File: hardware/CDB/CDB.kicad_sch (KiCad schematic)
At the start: 17 parts, among them J1 Servo Motor, J2 Bateria, J3 Antena LoRa, Q1 BC547, U1 ESP32-C3, U2 RFM95W, U3 GPS, U4 BMP280, U5 GY-521

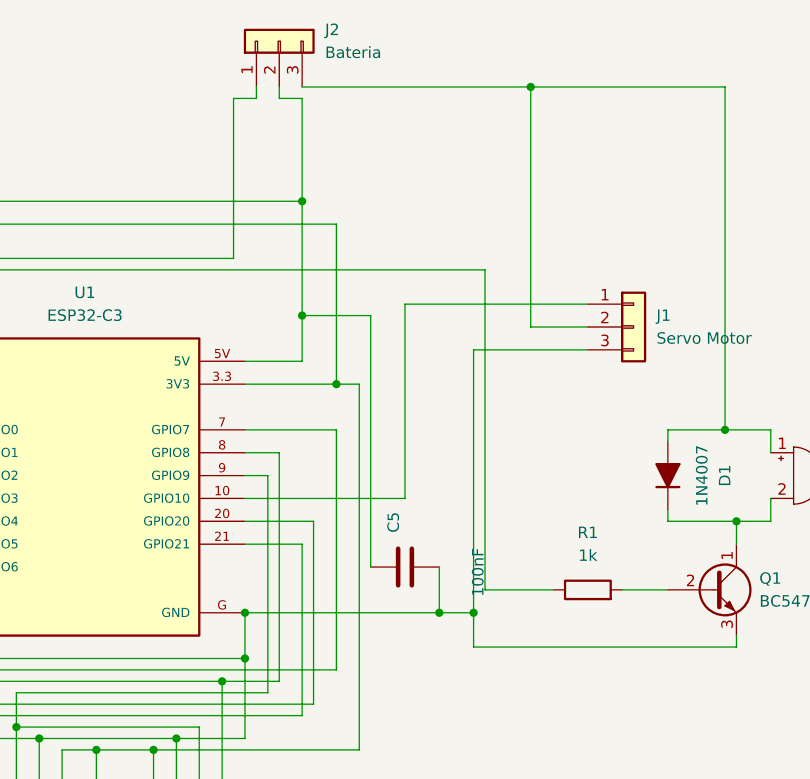
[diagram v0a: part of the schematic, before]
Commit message: add velocity threshold
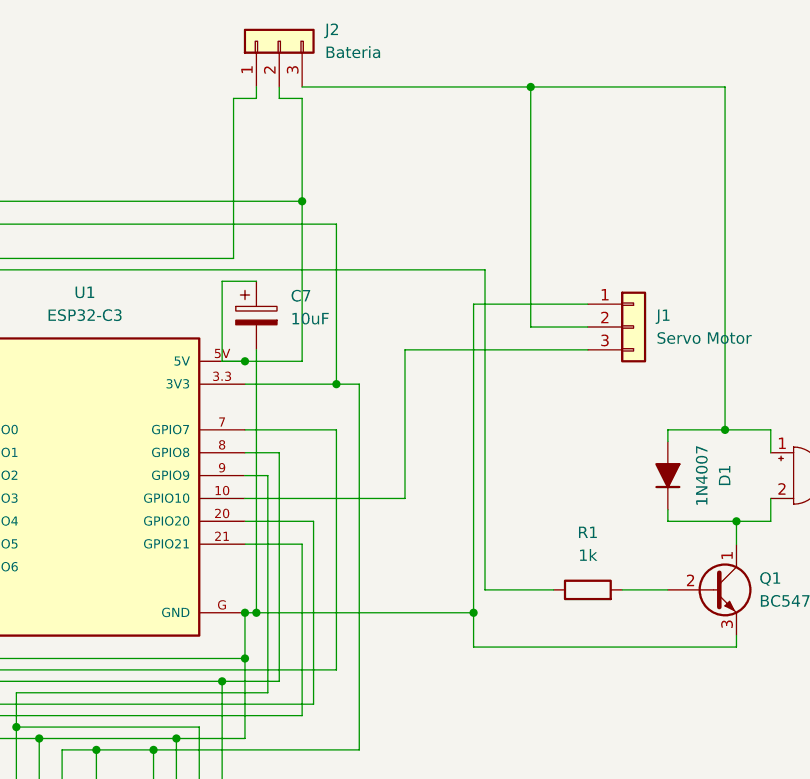
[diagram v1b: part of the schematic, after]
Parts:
- removed C5: 100nF, Capacitor_THT:C_Disc_D4.7mm_W2.5mm_P5.00mm, symbol PCM_Capacitor_AKL:C_Disc_D3.0mm_W1.6mm_P2.50mm
- added C7: 10uF, PCM_Capacitor_THT_AKL:CP_Radial_D4.0mm_P2.00mm, symbol PCM_Capacitor_AKL:CP_Radial_D4.0mm_P2.00mm
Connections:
- net at C1.2, C2.2, C3.2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: now also J1.1 (Pin_1), C7.2; no longer J1.3 (Pin_3)
- net at U1.10 (GPIO10): now also J1.3 (Pin_3); no longer J1.1 (Pin_1)
- net at C1.1, J2.2 (Pin_2), U1.5V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: now also C7.1
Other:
- company: (none) -> Serra Rocketry
- title: Aviônica SR1500 -> Aviônica SRCouto
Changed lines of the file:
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@@
 	(paper "A4")
 	(title_block
-		(title "Aviônica SR1500")
+		(title "Aviônica SRCouto")
 		(date "2025-06-04")
+		(company "Serra Rocketry")
 	)
 	(junction
@@
 	)
 	(junction
-		(at 167.64 71.12)
-		(diameter 0)
-		(color 0 0 0 0)
-	)
-	(junction
 		(at 167.64 58.42)
 		(diameter 0)
@@
 	)
 	(junction
-		(at 151.13 119.38)
+		(at 161.29 76.2)
 		(diameter 0)
 		(color 0 0 0 0)
 	)
 	(junction
-		(at 182.88 104.14)
+		(at 151.13 119.38)
 		(diameter 0)
 		(color 0 0 0 0)
@@
 	)
 	(junction
+		(at 162.56 104.14)
+		(diameter 0)
+		(color 0 0 0 0)
+	)
+	(junction
 		(at 144.78 119.38)
 		(diameter 0)
@@
 	(wire
 		(pts
+			(xy 193.04 72.39) (xy 199.39 72.39)
+		)
+		(stroke
+			(width 0)
+			(type default)
+		)
+	)
+	(wire
+		(pts
 			(xy 104.14 93.98) (xy 80.01 93.98)
 		)
@@
 	(wire
 		(pts
-			(xy 186.69 74.93) (xy 186.69 104.14)
+			(xy 162.56 74.93) (xy 162.56 104.14)
 		)
 		(stroke
@@
 	(wire
 		(pts
+			(xy 179.07 74.93) (xy 199.39 74.93)
+		)
+		(stroke
+			(width 0)
+			(type default)
+		)
+	)
+	(wire
+		(pts
 			(xy 151.13 119.38) (xy 151.13 125.73)
 		)
@@
 	(wire
 		(pts
-			(xy 179.07 91.44) (xy 179.07 69.85)
+			(xy 179.07 91.44) (xy 179.07 74.93)
 		)
 		(stroke
@@
 	(wire
 		(pts
-			(xy 175.26 99.06) (xy 175.26 71.12)
-		)
-		(stroke
-			(width 0)
-			(type default)
-		)
-	)
-	(wire
-		(pts
 			(xy 156.21 116.84) (xy 135.89 116.84)
 		)
@@
 	(wire
 		(pts
-			(xy 161.29 104.14) (xy 182.88 104.14)
-		)
-		(stroke
-			(width 0)
-			(type default)
-		)
-	)
-	(wire
-		(pts
-			(xy 167.64 58.42) (xy 167.64 71.12)
+			(xy 161.29 104.14) (xy 162.56 104.14)
 		)
 		(stroke
@@
 	(wire
 		(pts
-			(xy 179.07 69.85) (xy 199.39 69.85)
-		)
-		(stroke
-			(width 0)
-			(type default)
-		)
-	)
-	(wire
-		(pts
 			(xy 58.42 118.11) (xy 58.42 58.42)
 		)
@@
 	(wire
 		(pts
+			(xy 162.56 104.14) (xy 186.69 104.14)
+		)
+		(stroke
+			(width 0)
+			(type default)
+		)
+	)
+	(wire
+		(pts
 			(xy 138.43 127) (xy 138.43 137.16)
 		)
@@
 	(wire
 		(pts
+			(xy 186.69 69.85) (xy 199.39 69.85)
+		)
+		(stroke
+			(width 0)
+			(type default)
+		)
+	)
+	(wire
+		(pts
 			(xy 165.1 111.76) (xy 165.1 86.36)
 		)
@@
 	(wire
 		(pts
+			(xy 158.75 76.2) (xy 161.29 76.2)
+		)
+		(stroke
+			(width 0)
+			(type default)
+		)
+	)
+	(wire
+		(pts
 			(xy 160.02 64.77) (xy 119.38 64.77)
 		)
@@
 	(wire
 		(pts
+			(xy 158.75 67.31) (xy 158.75 76.2)
+		)
+		(stroke
+			(width 0)
+			(type default)
+		)
+	)
+	(wire
+		(pts
 			(xy 167.64 46.99) (xy 167.64 58.42)
 		)
@@
 	(wire
 		(pts
-			(xy 193.04 72.39) (xy 193.04 45.72)
-		)
-		(stroke
-			(width 0)
-			(type default)
-		)
-	)
-	(wire
-		(pts
 			(xy 63.5 99.06) (xy 118.11 99.06)
 		)
@@
 	(wire
 		(pts
+			(xy 186.69 69.85) (xy 186.69 104.14)
+		)
+		(stroke
+			(width 0)
+			(type default)
+		)
+	)
+	(wire
+		(pts
 			(xy 66.04 135.89) (xy 66.04 118.11)
 		)
@@
 	(wire
 		(pts
-			(xy 182.88 99.06) (xy 182.88 104.14)
-		)
-		(stroke
-			(width 0)
-			(type default)
-		)
-	)
-	(wire
-		(pts
 			(xy 59.69 73.66) (xy 59.69 101.6)
 		)
@@
 	(wire
 		(pts
-			(xy 199.39 74.93) (xy 186.69 74.93)
-		)
-		(stroke
-			(width 0)
-			(type default)
-		)
-	)
-	(wire
-		(pts
 			(xy 171.45 60.96) (xy 171.45 78.74)
 		)
@@
 	(wire
 		(pts
+			(xy 162.56 67.31) (xy 158.75 67.31)
+		)
+		(stroke
+			(width 0)
+			(type default)
+		)
+	)
+	(wire
+		(pts
 			(xy 167.64 45.72) (xy 193.04 45.72)
 		)
@@
 	(wire
 		(pts
-			(xy 175.26 71.12) (xy 167.64 71.12)
-		)
-		(stroke
-			(width 0)
-			(type default)
-		)
-	)
-	(wire
-		(pts
 			(xy 157.48 139.7) (xy 147.32 139.7)
 		)
@@
 	(wire
 		(pts
+			(xy 193.04 45.72) (xy 193.04 72.39)
+		)
+		(stroke
+			(width 0)
+			(type default)
+		)
+	)
+	(wire
+		(pts
 			(xy 165.1 135.89) (xy 153.67 135.89)
 		)
@@
 	(wire
 		(pts
-			(xy 199.39 72.39) (xy 193.04 72.39)
-		)
-		(stroke
-			(width 0)
-			(type default)
-		)
-	)
-	(wire
-		(pts
 			(xy 64.77 78.74) (xy 62.23 78.74)
 		)
@@
 	(wire
 		(pts
-			(xy 167.64 71.12) (xy 167.64 76.2)
+			(xy 167.64 58.42) (xy 167.64 76.2)
 		)
 		(stroke
@@
 		(pts
 			(xy 208.28 83.82) (xy 214.63 83.82)
-		)
-		(stroke
-			(width 0)
-			(type default)
-		)
-	)
-	(wire
-		(pts
-			(xy 182.88 104.14) (xy 186.69 104.14)
 		)
 		(stroke
@@
 	)
 	(symbol
+		(lib_id "PCM_Capacitor_AKL:CP_Radial_D4.0mm_P2.00mm")
+		(at 162.56 71.12 0)
+		(unit 1)
+		(exclude_from_sim no)
+		(in_bom yes)
+		(on_board yes)
+		(dnp no)
+		(fields_autoplaced yes)
+		(property "Reference" "C7"
+			(at 166.37 68.9609 0)
+			(effects
+				(font
+					(size 1.27 1.27)
+				)
+				(justify left)
+			)
+		)
+		(property "Value" "10uF"
+			(at 166.37 71.5009 0)
+			(effects
+				(font
+					(size 1.27 1.27)
+				)
+				(justify left)
+			)
+		)
+		(property "Footprint" "PCM_Capacitor_THT_AKL:CP_Radial_D4.0mm_P2.00mm"
+			(at 162.56 81.28 0)
+			(effects
+				(font
+					(size 1.27 1.27)
+				)
+				(hide yes)
+			)
+		)
+		(property "Datasheet" "~"
+			(at 162.56 71.12 0)
+			(effects
+				(font
+					(size 1.27 1.27)
+				)
+				(hide yes)
+			)
+		)
+		(property "Description" "THT Electrolytic Capacitor, 4.0mm Diameter, 2.00mm Pitch, European Symbol, Alternate KiCad Library"
+			(at 162.56 71.12 0)
+			(effects
+				(font
+					(size 1.27 1.27)
+				)
+				(hide yes)
+			)
+		)
+		(pin "2"
+		)
+		(pin "1"
+		)
+		(instances
+			(project ""
+				(path "/e713cbe1-3cec-4424-b31f-a0d8c786dd98"
+					(reference "C7")
+					(unit 1)
+				)
+			)
+		)
+	)
+	(symbol
 		(lib_id "Transistor_BJT:BC547")
 		(at 213.36 101.6 0)
@@
 					(unit 1)
 				)
-			)
-		)
-	)
-	(symbol
-		(lib_id "PCM_Capacitor_AKL:C_Disc_D3.0mm_W1.6mm_P2.50mm")
-		(at 179.07 99.06 90)
-		(unit 1)
-		(exclude_from_sim no)
-		(in_bom yes)
-		(on_board yes)
-		(dnp no)
-		(property "Reference" "C5"
-			(at 177.7999 95.25 0)
-			(effects
-				(font
-					(size 1.27 1.27)
-				)
-				(justify left)
-			)
-		)
-		(property "Value" "100nF"
-			(at 187.198 102.362 0)
-			(effects
-				(font
-					(size 1.27 1.27)
-				)
-				(justify left)
-			)
-		)
-		(property "Footprint" "Capacitor_THT:C_Disc_D4.7mm_W2.5mm_P5.00mm"
-			(at 182.88 98.0948 0)
-			(effects
-				(font
-					(size 1.27 1.27)
-				)
-				(hide yes)
-			)
-		)
-		(property "Datasheet" "~"
-			(at 179.07 99.06 0)
-			(effects
-				(font
-					(size 1.27 1.27)
-				)
-				(hide yes)
-			)
-		)
-		(property "Description" "THT Ceramic Disc Capacitor, 3.0mm Diameter, 1.6mm Width, 2.50mm Pitch, Alternate KiCad Library"
-			(at 179.07 99.06 0)
-			(effects
-				(font
-					(size 1.27 1.27)
-				)
-				(hide yes)
-			)
-		)
-		(pin "1"
-		)
-		(pin "2"
-		)
-		(instances
-			(project "CDB"
-				(path "/e713cbe1-3cec-4424-b31f-a0d8c786dd98"
-					(reference "C5")
-					(unit 1)
-				)
